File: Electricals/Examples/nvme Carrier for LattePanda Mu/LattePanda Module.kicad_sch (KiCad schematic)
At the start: 12 parts, among them J1 Conn_01x03_Pin

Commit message: Some small changes
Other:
- note added: "DDI/TCP functions are defined by the BIOS source code, Cannot be changed in BIOS settings. The functions are defined as follows: - DDIA: eDP 1.4b (the 40Pin connector on the Mu) - DDIB: HDMI 2.0 - TCP0: HDMI 2.0"
- note added: "HSIO functions are defined by the BIOS source code, Cannot be changed in BIOS settings. The functions are defined as follows: - HSIO0: USB3.2 10Gbps - HSIO1: PCIe 3.0 x1 M.2 - HSIO2: PCIe 3.0 x1 M.2 - HSIO3: PCIe 3.0 x1 M.2 - HSIO8: PCIe 3.0 x1 M.2 - HSIO9: PCIe 3.0 x1 M.2 - HSIO10: PCIe 3.0 x1 M.2 - HSIO11: PCIe 3.0 x4 (Lane 1) - HSIO6: PCIe 3.0 x4 (Lane 1)"
- note removed: "DDI/TCP functions are defined by the BIOS source code, Cannot be changed in BIOS settings. Before starting design, you should choose one of the available BIOS configurations on: https://github.com/LattePandaTeam/LattePanda-Mu The default functions are defined as follows: - DDIA: eDP 1.4b (the 40Pin connector on the Mu) - DDIB: HDMI 2.0 - TCP0: HDMI 2.0 - TCP1: USB TypeC (need external PD controll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"
- note removed: "HSIO functions are defined by the BIOS source code, Cannot be changed in BIOS settings. Before starting design, you should choose one of the available BIOS configurations on: https://github.com/LattePandaTeam/LattePanda-Mu Or contact techsupport for custom your BIOS The default functions are defined as follows: - HSIO0: USB3.2 10Gbps - HSIO1: PCIe 3.0 x1 M.2 - HSIO2: PCIe 3.0 x1 M.2 - HSIO3: PCIe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"
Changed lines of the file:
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@@
 		)
 	)
-	(text_box "HSIO_1 used for USB3.0 \n"
+	(text_box "HSIO_0 used for USB3.0 \n"
 		(exclude_from_sim no)
 		(at 175.26 82.55 0)
@@
 		)
 	)
-	(text_box "HSIO_0, 2, 3, 8, 9 and 10 used for M.2 M KEY\n"
+	(text_box "HSIO_1, 2, 3, 8, 9 and 10 used for M.2 M KEY\n"
 		(exclude_from_sim no)
 		(at 175.26 96.52 0)
@@
 		)
 	)
-	(text "HSIO functions are defined by the BIOS source code, \nCannot be changed in BIOS settings.\n\nBefore starting design, you should choose one of\nthe available BIOS configurations on:\nhttps://github.com/LattePandaTeam/LattePanda-Mu\nOr contact techsupport for custom your BIOS\n\nThe default functions are defined as follows:\n\n- HSIO0: USB3.2 10Gbps\n- HSIO1: PCIe 3.0 x1 M.2\n- HSIO2: PCIe 3.0 x1 M.2\n- HSIO3: PCIe 3.0 x1 M.2\n\n- HSIO8: PCIe 3.0 x1 M.2\n- HSIO9: PCIe 3.0 x1 M.2\n- HSIO10: PCIe 3.0 x1 M.2\n- HSIO11: PCIe 3.0 x4 (Lane 1)\n\n- HSIO6: PCIe 3.0 x4 (Lane 1)"
+	(text "HSIO functions are defined by the BIOS source code, \nCannot be changed in BIOS settings.\n\nThe functions are defined as follows:\n\n- HSIO0:  USB3.2 10Gbps\n- HSIO1:  PCIe 3.0 x1 M.2\n- HSIO2:  PCIe 3.0 x1 M.2\n- HSIO3:  PCIe 3.0 x1 M.2\n\n- HSIO8:  PCIe 3.0 x1 M.2\n- HSIO9:  PCIe 3.0 x1 M.2\n- HSIO10: PCIe 3.0 x1 M.2\n- HSIO11: PCIe 3.0 x4 (Lane 1)\n\n- HSIO6:  PCIe 3.0 x4 (Lane 1)"
 		(exclude_from_sim no)
 		(at 50.8 88.9 0)
@@
 		)
 	)
-	(text "DDI/TCP functions are defined by the BIOS source code, \nCannot be changed in BIOS settings.\n\nBefore starting design, you should choose one of\nthe available BIOS configurations on:\nhttps://github.com/LattePandaTeam/LattePanda-Mu\n\nThe default functions are defined as follows:\n\n- DDIA: eDP 1.4b (the 40Pin connector on the Mu)\n\n- DDIB: HDMI 2.0\n\n- TCP0: HDMI 2.0\n\n- TCP1: USB TypeC (need external PD controller)"
+	(text "DDI/TCP functions are defined by the BIOS source code, \nCannot be changed in BIOS settings.\n\nThe functions are defined as follows:\n\n- DDIA: eDP 1.4b (the 40Pin connector on the Mu)\n\n- DDIB: HDMI 2.0\n\n- TCP0: HDMI 2.0"
 		(exclude_from_sim no)
 		(at 50.8 215.9 0)

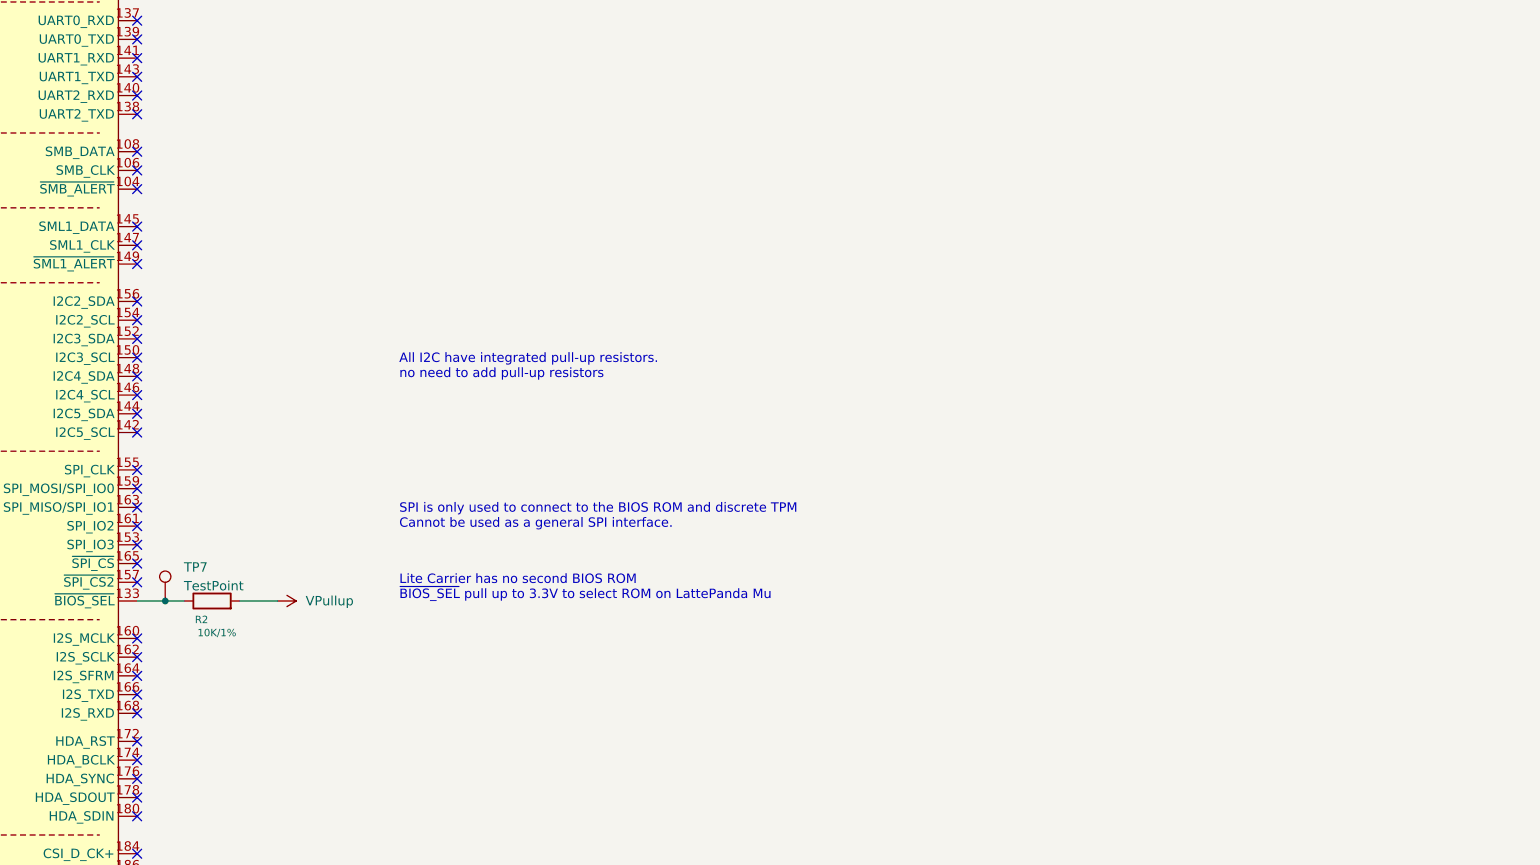
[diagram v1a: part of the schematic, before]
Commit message: Add BIOS Chip to Carrier
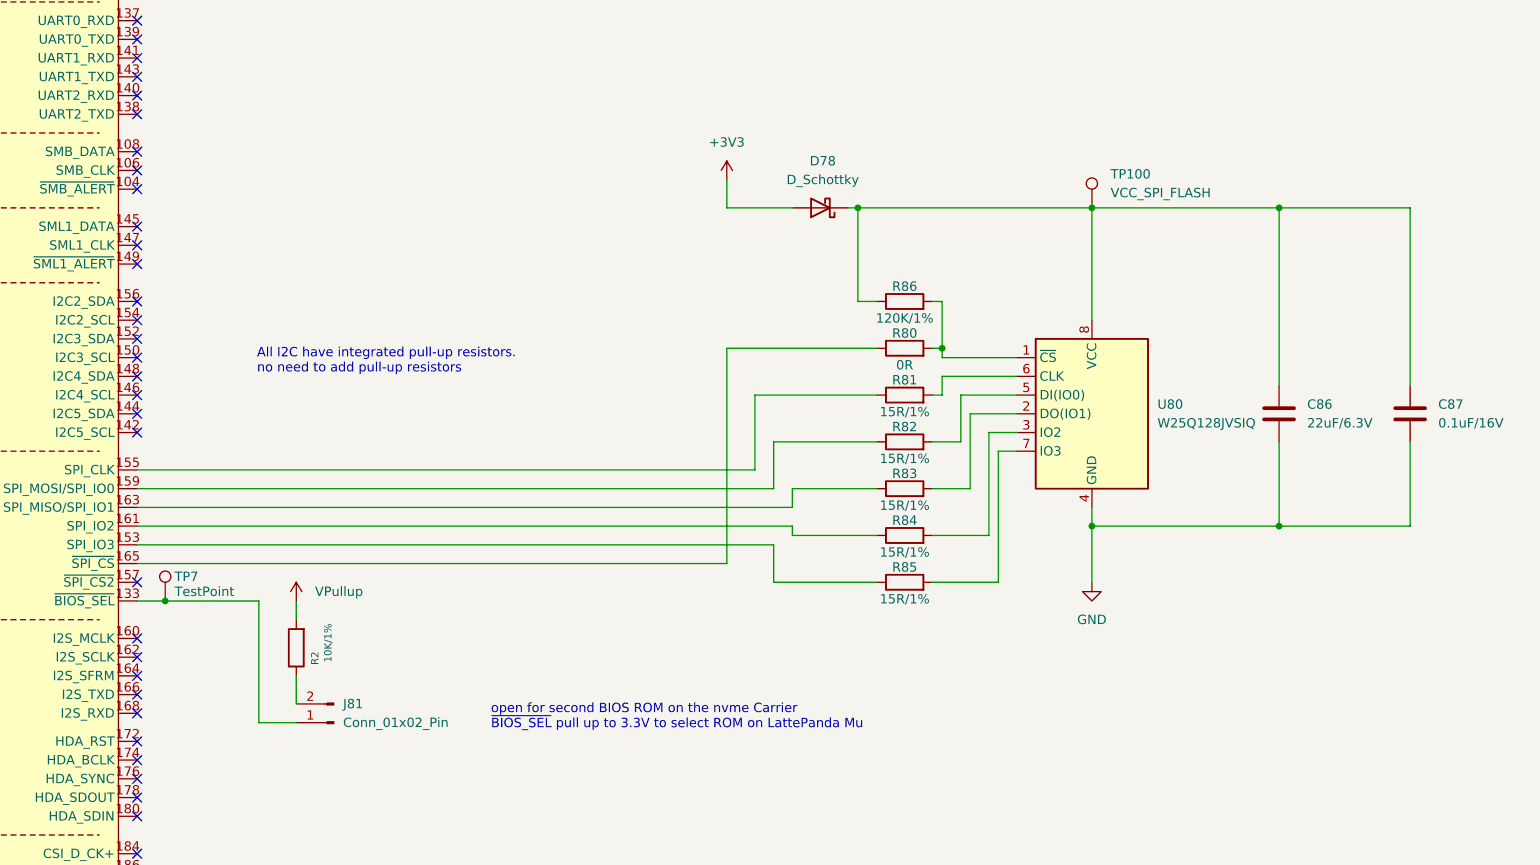
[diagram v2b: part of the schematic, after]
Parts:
- added C86: 22uF/6.3V, A_HDJ_Library:C_0402_1005Metric, symbol Device:C
- added C87: 0.1uF/16V, A_HDJ_Library:C_0402_1005Metric, symbol Device:C
- added D78: D_Schottky, Diode_SMD:D_SOD-923, symbol Device:D_Schottky
- added J81: Conn_01x02_Pin, Connector_PinHeader_2.54mm:PinHeader_1x02_P2.54mm_Vertical, symbol Connector:Conn_01x02_Pin
- added R80: 0R, A_HDJ_Library:R_0402_1005Metric, symbol Device:R
- added R81, R82, R83, R84, R85: 15R/1%, A_HDJ_Library:R_0402_1005Metric, symbol Device:R
- added R86: 120K/1%, A_HDJ_Library:R_0402_1005Metric, symbol Device:R
- added TP100: VCC_SPI_FLASH, A_HDJ_Library:TestPoint_Pad_D1.5mm, symbol Connector:TestPoint
- added U80: W25Q128JVSIQ, Package_SO:SOIC-8_5.23x5.23mm_P1.27mm, symbol Memory_Flash:W25Q128JVS
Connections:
- net GND: now also C86.2, C87.2, U80.4 (GND)
- net at A1.133 (~{BIOS_SEL}), TP7.1: now also J81.1 (Pin_1); no longer R2.1
- net at A1.153 (SPI_IO3): now also R85.1
- net at A1.155 (SPI_CLK): now also R81.1
- net at A1.159 (SPI_MOSI/SPI_IO0): now also R82.1
- net at A1.161 (SPI_IO2): now also R84.1
- net at A1.163 (SPI_MISO/SPI_IO1): now also R83.1
- net at A1.165 (~{SPI_CS}): now also R80.1
- new net: R82.2, U80.5 (DI(IO0))
- new net: R84.2, U80.3 (IO2)
- new net: C86.1, C87.1, D78.1 (K), R86.1, TP100.1, U80.8 (VCC)
- new net: R80.2, R86.2, U80.1 (~{CS})
- new net: R83.2, U80.2 (DO(IO1))
- new net: R81.2, U80.6 (CLK)
- new net: R85.2, U80.7 (IO3)
- new net: J81.2 (Pin_2), R2.1
- new net +3V3: D78.2 (A)
- no-connect marks 102 -> 96
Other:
- note added: "open for second BIOS ROM on the nvme Carrier ~{BIOS_SEL} pull up to 3.3V to select ROM on LattePanda Mu"
- note removed: "Lite Carrier has no second BIOS ROM ~{BIOS_SEL} pull up to 3.3V to select ROM on LattePanda Mu"
- note removed: "SPI is only used to connect to the BIOS ROM and discrete TPM Cannot be used as a general SPI interface."
- moved on the sheet: R2

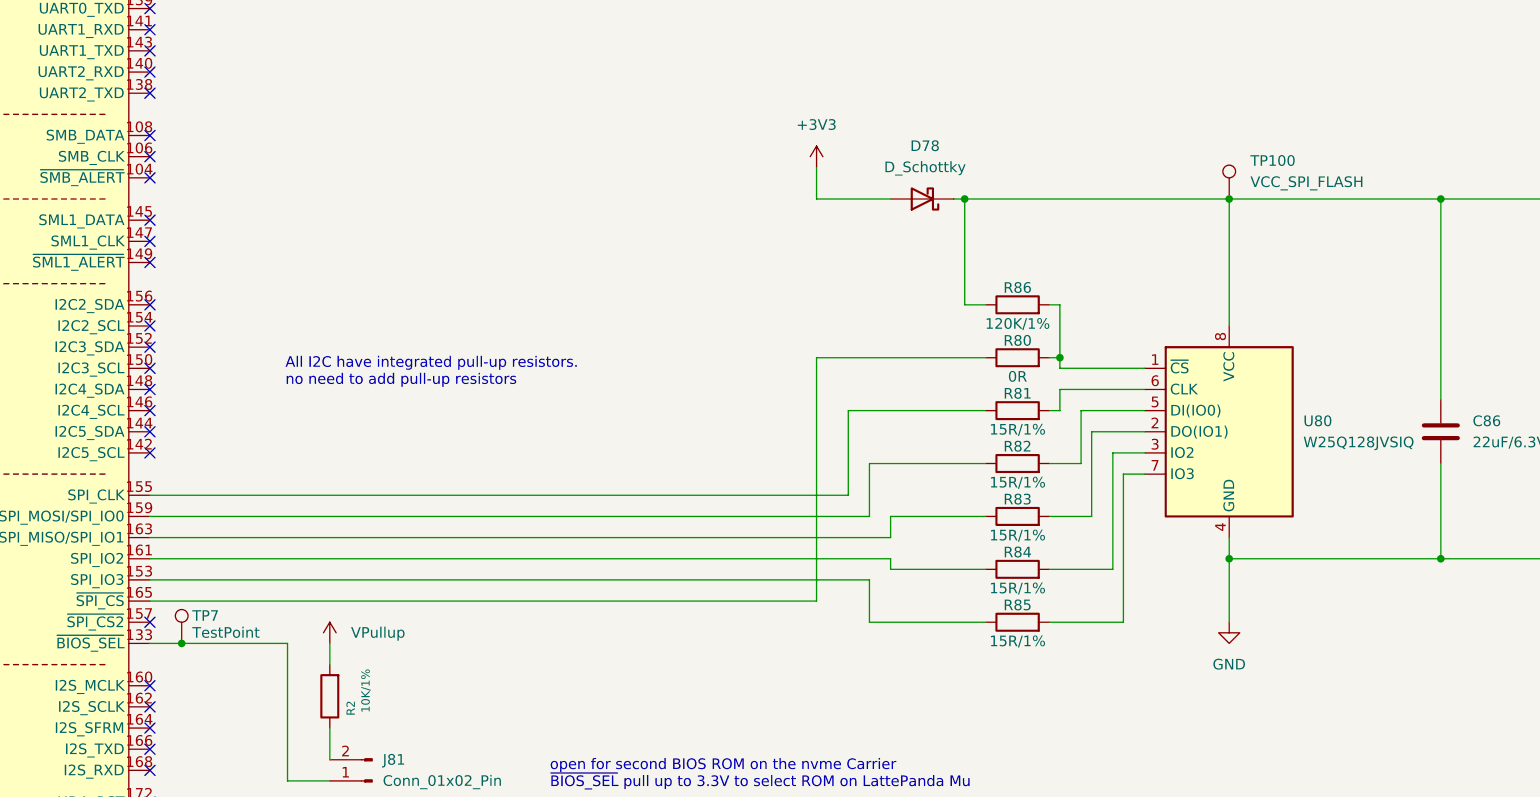
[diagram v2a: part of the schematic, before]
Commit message: Add BIOS Chip and small Changes to the Board
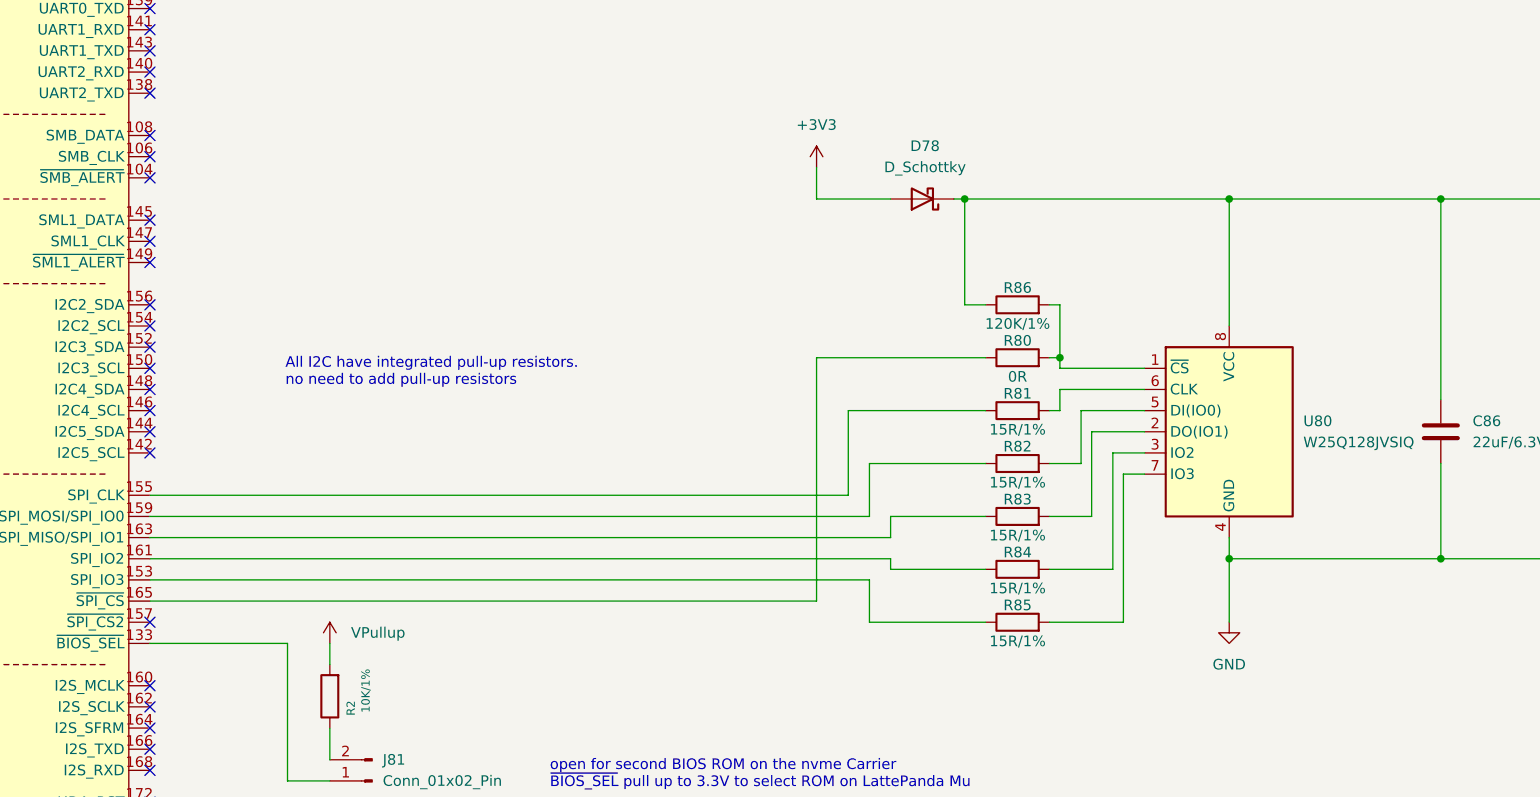
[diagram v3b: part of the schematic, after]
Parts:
- removed TP100: VCC_SPI_FLASH, A_HDJ_Library:TestPoint_Pad_D1.5mm, symbol Connector:TestPoint
- removed TP7: TestPoint, A_HDJ_Library:TestPoint_Pad_D1.5mm, symbol Connector:TestPoint
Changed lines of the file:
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@@
 	)
 	(junction
-		(at 355.6 256.54)
-		(diameter 0)
-		(color 0 0 0 0)
-	)
-	(junction
 		(at 313.69 44.45)
 		(diameter 0)
@@
 	(wire
 		(pts
-			(xy 351.79 256.54) (xy 355.6 256.54)
+			(xy 351.79 256.54) (xy 368.3 256.54)
 		)
 		(stroke
@@
 	(wire
 		(pts
-			(xy 355.6 256.54) (xy 368.3 256.54)
-		)
-		(stroke
-			(width 0)
-			(type default)
-		)
-	)
-	(wire
-		(pts
 			(xy 351.79 90.17) (xy 369.57 90.17)
 		)
@@
 	)
 	(symbol
-		(lib_id "Connector:TestPoint")
-		(at 481.33 203.2 0)
-		(unit 1)
-		(exclude_from_sim no)
-		(in_bom no)
-		(on_board yes)
-		(dnp no)
-		(fields_autoplaced yes)
-		(property "Reference" "TP100"
-			(at 483.87 198.6279 0)
-			(effects
-				(font
-					(size 1.27 1.27)
-				)
-				(justify left)
-			)
-		)
-		(property "Value" "VCC_SPI_FLASH"
-			(at 483.87 201.1679 0)
-			(effects
-				(font
-					(size 1.27 1.27)
-				)
-				(justify left)
-			)
-		)
-		(property "Footprint" "A_HDJ_Library:TestPoint_Pad_D1.5mm"
-			(at 486.41 203.2 0)
-			(effects
-				(font
-					(size 1.27 1.27)
-				)
-				(hide yes)
-			)
-		)
-		(property "Datasheet" "~"
-			(at 486.41 203.2 0)
-			(effects
-				(font
-					(size 1.27 1.27)
-				)
-				(hide yes)
-			)
-		)
-		(property "Description" "test point"
-			(at 481.33 203.2 0)
-			(effects
-				(font
-					(size 1.27 1.27)
-				)
-				(hide yes)
-			)
-		)
-		(property "Sim.Device" ""
-			(at 481.33 203.2 0)
-			(effects
-				(font
-					(size 1.27 1.27)
-				)
-				(hide yes)
-			)
-		)
-		(property "Sim.Pins" ""
-			(at 481.33 203.2 0)
-			(effects
-				(font
-					(size 1.27 1.27)
-				)
-				(hide yes)
-			)
-		)
-		(property "Sim.Type" ""
-			(at 481.33 203.2 0)
-			(effects
-				(font
-					(size 1.27 1.27)
-				)
-				(hide yes)
-			)
-		)
-		(pin "1"
-		)
-		(instances
-			(project "nvme Carrier for LattePanda Mu"
-				(path "/2a6d114a-7fd7-4207-b5f7-4ea9c34f36aa/6eee02c2-78c9-4e83-9ccf-e0f7690b57bf"
-					(reference "TP100")
-					(unit 1)
-				)
-			)
-		)
-	)
-	(symbol
 		(lib_id "Device:R")
 		(at 406.4 120.65 0)
@@
 					(unit 1)
 				)
-			)
-		)
-	)
-	(symbol
-		(lib_id "Connector:TestPoint")
-		(at 355.6 256.54 0)
-		(unit 1)
-		(exclude_from_sim no)
-		(in_bom no)
-		(on_board yes)
-		(dnp no)
-		(property "Reference" "TP7"
-			(at 356.87 253.238 0)
-			(effects
-				(font
-					(size 1.27 1.27)
-				)
-				(justify left)
-			)
-		)
-		(property "Value" "TestPoint"
-			(at 356.87 255.27 0)
-			(effects
-				(font
-					(size 1.27 1.27)
-				)
-				(justify left)
-			)
-		)
-		(property "Footprint" "A_HDJ_Library:TestPoint_Pad_D1.5mm"
-			(at 360.68 256.54 0)
-			(effects
-				(font
-					(size 1.27 1.27)
-				)
-				(hide yes)
-			)
-		)
-		(property "Datasheet" "~"
-			(at 360.68 256.54 0)
-			(effects
-				(font
-					(size 1.27 1.27)
-				)
-				(hide yes)
-			)
-		)
-		(property "Description" "test point"
-			(at 355.6 256.54 0)
-			(effects
-				(font
-					(size 1.27 1.27)
-				)
-				(hide yes)
-			)
-		)
-		(property "Sim.Device" ""
-			(at 355.6 256.54 0)
-			(effects
-				(font
-					(size 1.27 1.27)
-				)
-				(hide yes)
-			)
-		)
-		(property "Sim.Pins" ""
-			(at 355.6 256.54 0)
-			(effects
-				(font
-					(size 1.27 1.27)
-				)
-				(hide yes)
-			)
-		)
-		(property "Sim.Type" ""
-			(at 355.6 256.54 0)
-			(effects
-				(font
-					(size 1.27 1.27)
-				)
-				(hide yes)
-			)
-		)
-		(pin "1"
-		)
-		(instances
-			(project "nvme Carrier for LattePanda Mu"
-				(path "/2a6d114a-7fd7-4207-b5f7-4ea9c34f36aa/6eee02c2-78c9-4e83-9ccf-e0f7690b57bf"
-					(reference "TP7")
-					(unit 1)
-				)
